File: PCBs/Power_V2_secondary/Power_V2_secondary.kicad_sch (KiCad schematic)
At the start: 9 parts, among them IC7 ACS712ELCTR-20A-T, J1 PCIE-164-02-F-D-TH-TR, J15 YK4420203000G, J8 Conn_01x02, U2 178.6164.0001

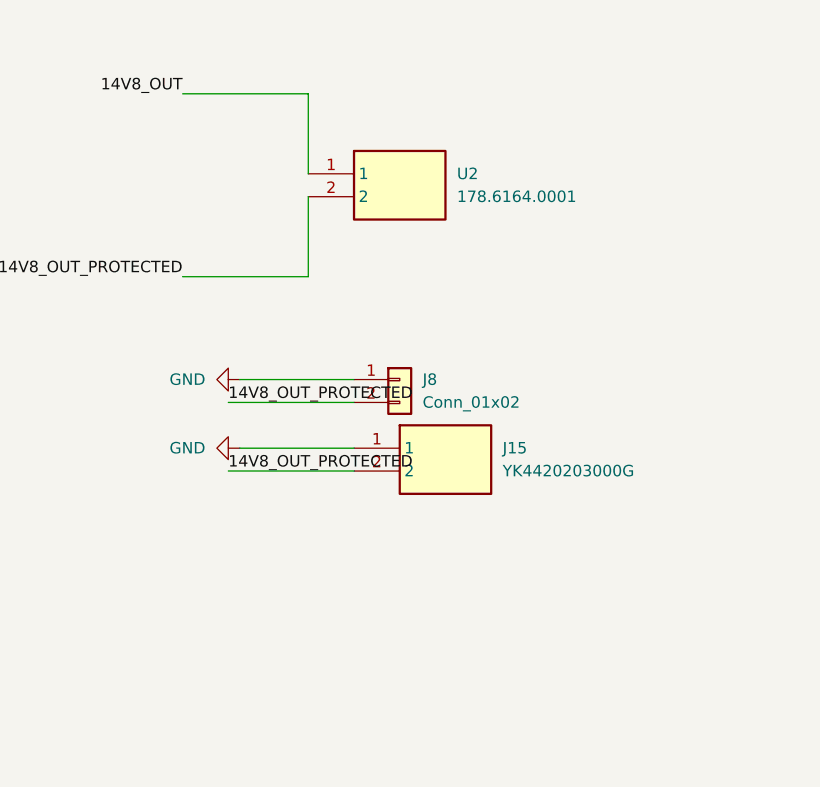
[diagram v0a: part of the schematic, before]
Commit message: shortened main board and secondary
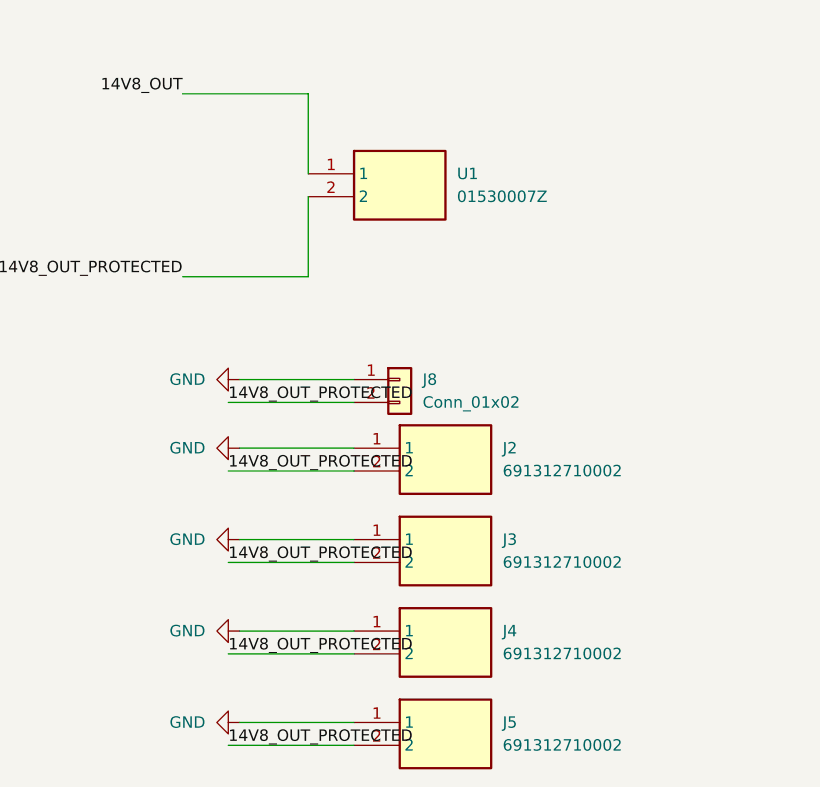
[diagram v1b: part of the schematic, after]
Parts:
- removed J15: YK4420203000G, iprl_footprints:RHDR2W120P0X950_1X2_2050X1430X1790P, symbol YK4420203000G:YK4420203000G
- removed U2: 178.6164.0001, iprl_footprints:178.6164.XXX1, symbol 178_6164_0001:178.6164.0001
- added J2, J3, J4, J5: 691312710002, iprl_footprints:SHDR2W100P0X500_1X2_1000X1200X850P, symbol 691312710002:691312710002
- added U1: 01530007Z, iprl_footprints:01530007Z, symbol 01530007Z:01530007Z
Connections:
- net 14V8_OUT: now also U1.1
- net 14V8_OUT_PROTECTED: now also J2.2, J3.2, J4.2, J5.2, U1.2
- net GND: now also J2.1, J3.1, J4.1, J5.1

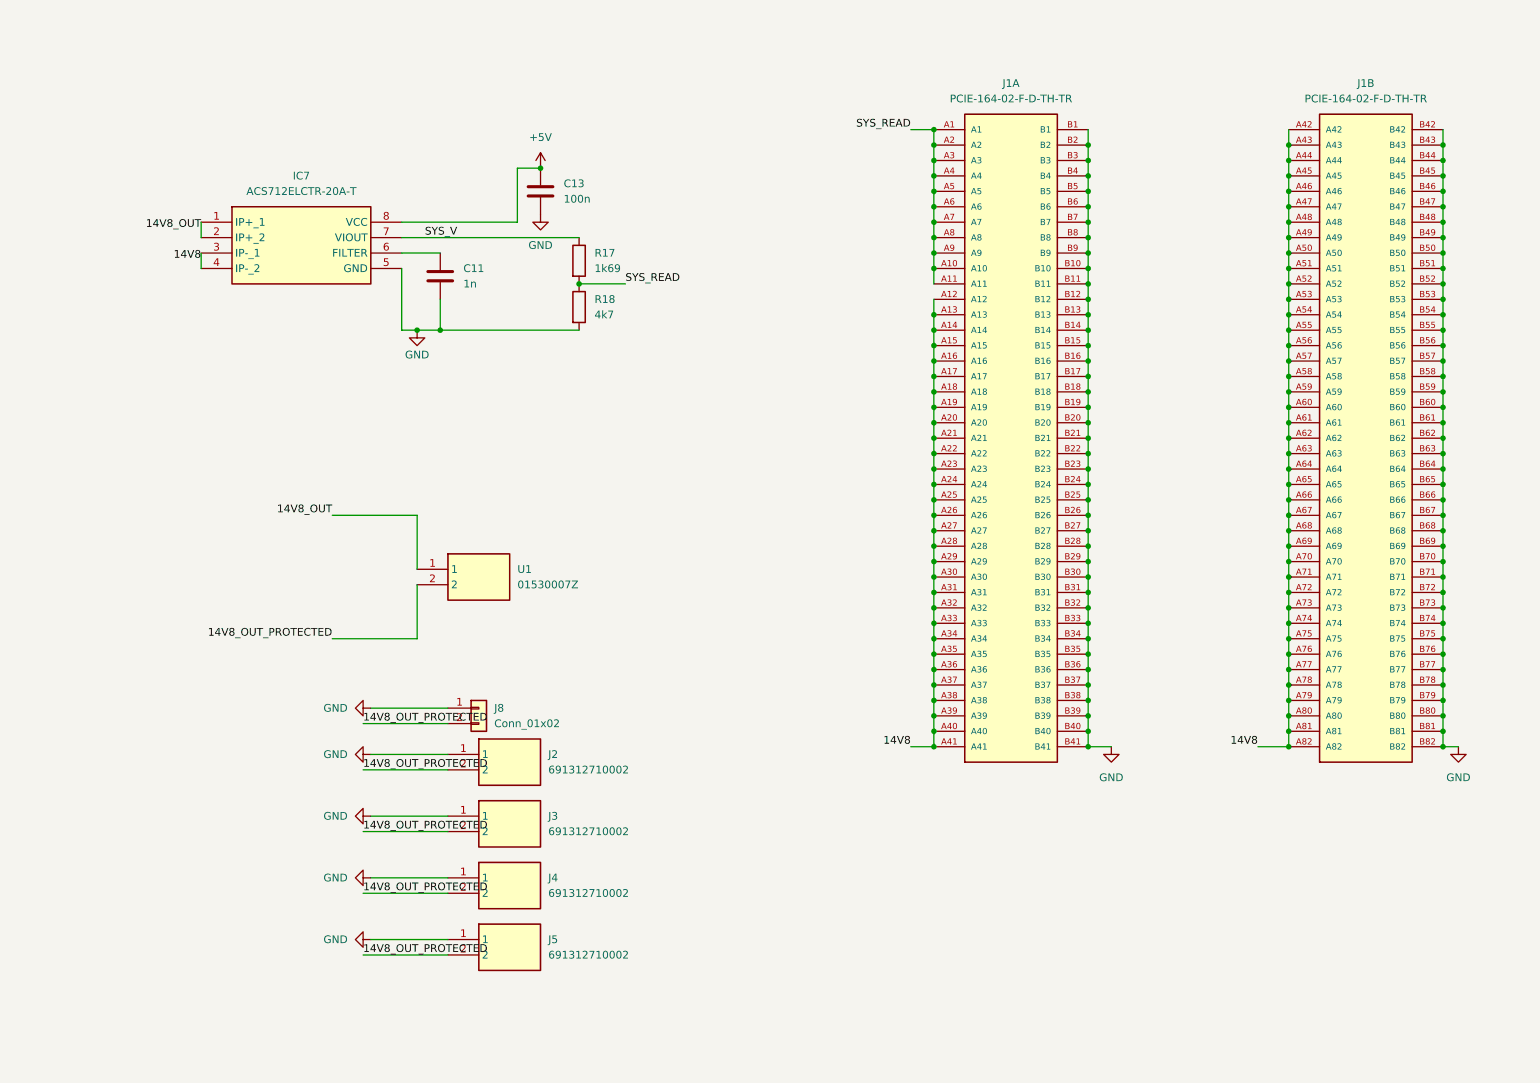
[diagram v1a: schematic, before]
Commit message: LEDs added to secondary
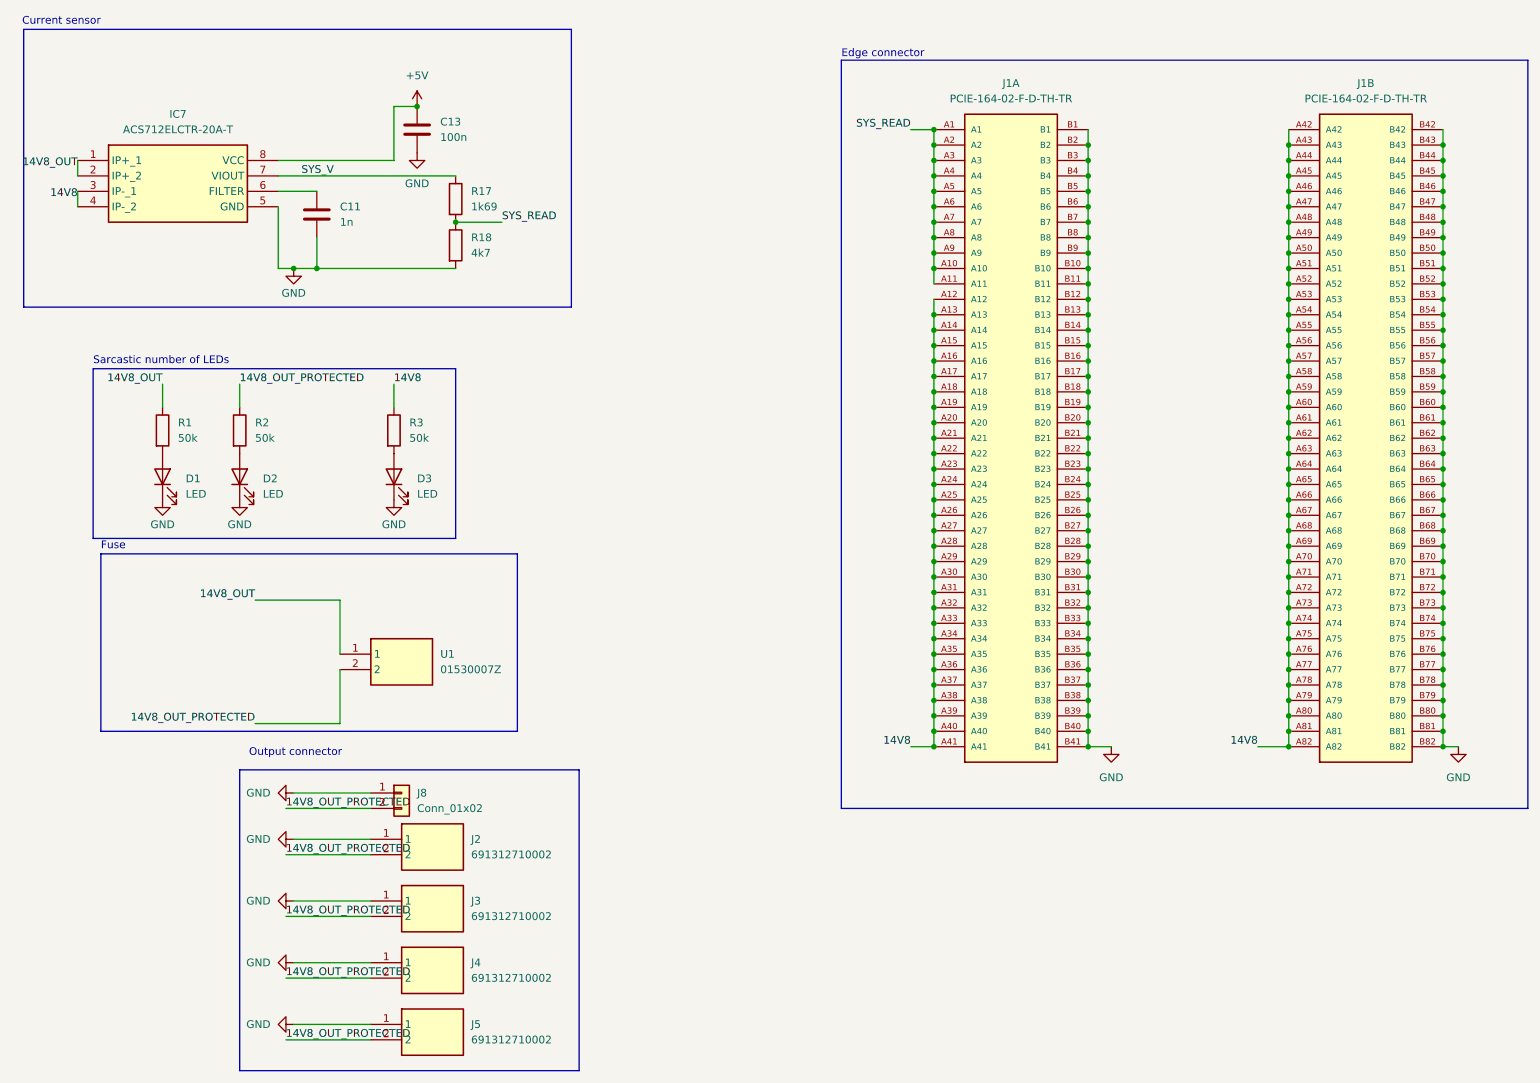
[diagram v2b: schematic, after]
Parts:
- added D1, D2, D3: LED, Diode_SMD:D_0805_2012Metric, symbol Device:LED
- added R1, R2, R3: 50k, Resistor_SMD:R_0805_2012Metric, symbol Device:R
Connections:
- net 14V8: now also R3.1
- net 14V8_OUT: now also R1.1
- net 14V8_OUT_PROTECTED: now also R2.1
- net GND: now also D1.1 (K), D2.1 (K), D3.1 (K)
- new net: D1.2 (A), R1.2
- new net: D3.2 (A), R3.2
- new net: D2.2 (A), R2.2
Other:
- note added: "Current sensor"
- note added: "Edge connector"
- note added: "Fuse"
- note added: "Output connector"
- note added: "Sarcastic number of LEDs"
- moved on the sheet: C11, C13, IC7, J2, J3, J4, J5, J8, R17, R18, U1

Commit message: added LED indicators to board and redid power distribution in PCIe
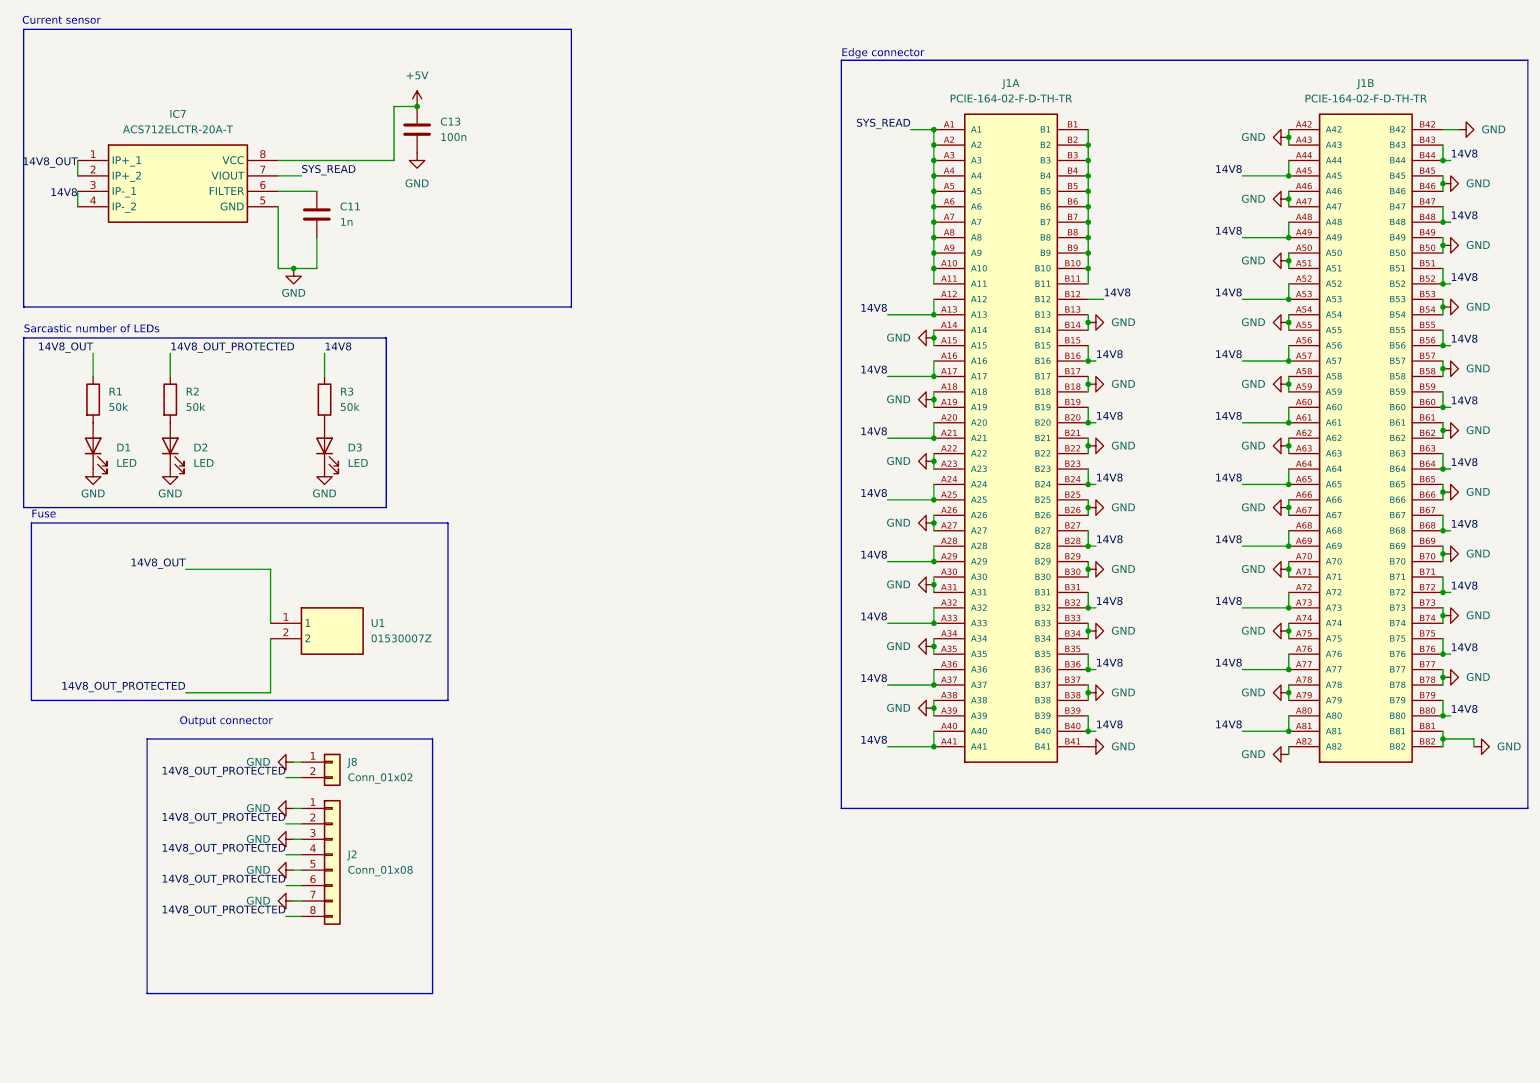
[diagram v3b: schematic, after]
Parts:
- removed J2, J3, J4, J5: 691312710002, iprl_footprints:SHDR2W100P0X500_1X2_1000X1200X850P, symbol 691312710002:691312710002
- removed R17: 1k69, Resistor_SMD:R_0805_2012Metric, symbol Device:R
- removed R18: 4k7, Resistor_SMD:R_0805_2012Metric, symbol Device:R
- added J2: Conn_01x08, TerminalBlock:TerminalBlock_MaiXu_MX126-5.0-08P_1x08_P5.00mm, symbol Connector_Generic:Conn_01x08
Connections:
- net SYS_V is gone; now on net SYS_READ: IC7.7 (VIOUT)
- net 14V8: now also J1.B12, J1.B15, J1.B16, J1.B19, J1.B20, J1.B23, J1.B24, J1.B27, J1.B28, J1.B31, J1.B32, J1.B35, J1.B36, J1.B39, J1.B40, J1.B43, J1.B44, J1.B47, J1.B48, J1.B51, J1.B52, J1.B55, J1.B56, J1.B59, J1.B60, J1.B63, J1.B64, J1.B67, J1.B68, J1.B71, J1.B72, J1.B75, J1.B76, J1.B79, J1.B80; no longer J1.A14, J1.A15, J1.A18, J1.A19, J1.A22, J1.A23, J1.A26, J1.A27, J1.A30, J1.A31, J1.A34, J1.A35, J1.A38, J1.A39, J1.A42, J1.A43, J1.A46, J1.A47, J1.A50, J1.A51, J1.A54, J1.A55, J1.A58, J1.A59, J1.A62, J1.A63, J1.A66, J1.A67, J1.A70, J1.A71, J1.A74, J1.A75, J1.A78, J1.A79, J1.A82
- net 14V8_OUT_PROTECTED: now also J2.2 (Pin_2), J2.4 (Pin_4), J2.6 (Pin_6), J2.8 (Pin_8)
- net GND: now also J1.A14, J1.A15, J1.A18, J1.A19, J1.A22, J1.A23, J1.A26, J1.A27, J1.A30, J1.A31, J1.A34, J1.A35, J1.A38, J1.A39, J1.A42, J1.A43, J1.A46, J1.A47, J1.A50, J1.A51, J1.A54, J1.A55, J1.A58, J1.A59, J1.A62, J1.A63, J1.A66, J1.A67, J1.A70, J1.A71, J1.A74, J1.A75, J1.A78, J1.A79, J1.A82, J2.1 (Pin_1), J2.3 (Pin_3), J2.5 (Pin_5), J2.7 (Pin_7); no longer J1.B1, J1.B10, J1.B11, J1.B12, J1.B15, J1.B16, J1.B19, J1.B2, J1.B20, J1.B23, J1.B24, J1.B27, J1.B28, J1.B3, J1.B31, J1.B32, J1.B35, J1.B36, J1.B39, J1.B4, J1.B40, J1.B43, J1.B44, J1.B47, J1.B48, J1.B5, J1.B51, J1.B52, J1.B55, J1.B56, J1.B59, J1.B6, J1.B60, J1.B63, J1.B64, J1.B67, J1.B68, J1.B7, J1.B71, J1.B72, J1.B75, J1.B76, J1.B79, J1.B8, J1.B80, J1.B9
- new net: J1.B1, J1.B10, J1.B11, J1.B2, J1.B3, J1.B4, J1.B5, J1.B6, J1.B7, J1.B8, J1.B9
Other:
- moved on the sheet: D1, D2, D3, J8, R1, R2, R3, U1

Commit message: added mounting holes to secondary
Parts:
- added H1, H2: MountingHole, MountingHole:MountingHole_2.5mm, symbol Mechanical:MountingHole
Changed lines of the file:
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@@
+	)
+	(symbol
+		(lib_id "Mechanical:MountingHole")
+		(at 107.95 80.01 0)
+		(unit 1)
+		(exclude_from_sim no)
+		(in_bom no)
+		(on_board yes)
+		(dnp no)
+		(fields_autoplaced yes)
+		(property "Reference" "H2"
+			(at 110.49 78.7399 0)
+			(effects
+				(font
+					(size 1.27 1.27)
+				)
+				(justify left)
+			)
+		)
+		(property "Value" "MountingHole"
+			(at 110.49 81.2799 0)
+			(effects
+				(font
+					(size 1.27 1.27)
+				)
+				(justify left)
+			)
+		)
+		(property "Footprint" "MountingHole:MountingHole_2.5mm"
+			(at 107.95 80.01 0)
+			(effects
+				(font
+					(size 1.27 1.27)
+				)
+				(hide yes)
+			)
+		)
+		(property "Datasheet" "~"
+			(at 107.95 80.01 0)
+			(effects
+				(font
+					(size 1.27 1.27)
+				)
+				(hide yes)
+			)
+		)
+		(property "Description" "Mounting Hole without connection"
+			(at 107.95 80.01 0)
+			(effects
+				(font
+					(size 1.27 1.27)
+				)
+				(hide yes)
+			)
+		)
+		(instances
+			(project "Power_V2_secondary"
+				(path "/5d5051fd-2bba-4f17-ac84-ab8502b20b0d"
+					(reference "H2")
+					(unit 1)
+				)
+			)
+		)
 	)
 	(symbol
@@
 					(unit 1)
 				)
+			)
+		)
+	)
+	(symbol
+		(lib_id "Mechanical:MountingHole")
+		(at 92.71 80.01 0)
+		(unit 1)
+		(exclude_from_sim no)
+		(in_bom no)
+		(on_board yes)
+		(dnp no)
+		(fields_autoplaced yes)
+		(property "Reference" "H1"
+			(at 95.25 78.7399 0)
+			(effects
+				(font
+					(size 1.27 1.27)
+				)
+				(justify left)
+			)
+		)
+		(property "Value" "MountingHole"
+			(at 95.25 81.2799 0)
+			(effects
+				(font
+					(size 1.27 1.27)
+				)
+				(justify left)
+			)
+		)
+		(property "Footprint" "MountingHole:MountingHole_2.5mm"
+			(at 92.71 80.01 0)
+			(effects
+				(font
+					(size 1.27 1.27)
+				)
+				(hide yes)
+			)
+		)
+		(property "Datasheet" "~"
+			(at 92.71 80.01 0)
+			(effects
+				(font
+					(size 1.27 1.27)
+				)
+				(hide yes)
+			)
+		)
+		(property "Description" "Mounting Hole without connection"
+			(at 92.71 80.01 0)
+			(effects
+				(font
+					(size 1.27 1.27)
+				)
+				(hide yes)
+			)
+		)
+		(instances
+			(project "Power_V2_secondary"
+				(path "/5d5051fd-2bba-4f17-ac84-ab8502b20b0d"
+					(reference "H1")
+					(unit 1)
+				)

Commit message: Changes from meeting
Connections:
- net GND: now also J1.B1, J1.B10, J1.B11, J1.B2, J1.B3, J1.B4, J1.B5, J1.B6, J1.B7, J1.B8, J1.B9
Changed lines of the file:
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@@
 	)
 	(junction
+		(at 193.04 33.02)
+		(diameter 0)
+		(color 0 0 0 0)
+	)
+	(junction
 		(at 167.64 128.27)
 		(diameter 0)
@@
 	(wire
 		(pts
-			(xy 193.04 40.64) (xy 193.04 43.18)
+			(xy 167.64 111.76) (xy 167.64 114.3)
 		)
 		(stroke
@@
 	(wire
 		(pts
-			(xy 167.64 111.76) (xy 167.64 114.3)
+			(xy 251.46 101.6) (xy 251.46 102.87)
 		)
 		(stroke
@@
 	(wire
 		(pts
-			(xy 251.46 101.6) (xy 251.46 102.87)
+			(xy 193.04 74.93) (xy 193.04 76.2)
 		)
 		(stroke
@@
 	(wire
 		(pts
-			(xy 193.04 74.93) (xy 193.04 76.2)
+			(xy 251.46 76.2) (xy 251.46 78.74)
 		)
 		(stroke
@@
 	(wire
 		(pts
-			(xy 251.46 76.2) (xy 251.46 78.74)
+			(xy 193.04 33.02) (xy 195.58 33.02)
 		)
 		(stroke
@@
 	(wire
 		(pts
+			(xy 193.04 38.1) (xy 193.04 40.64)
+		)
+		(stroke
+			(width 0)
+			(type default)
+		)
+	)
+	(wire
+		(pts
 			(xy 226.06 105.41) (xy 226.06 106.68)
 		)
@@
 	(wire
 		(pts
+			(xy 193.04 50.8) (xy 193.04 53.34)
+		)
+		(stroke
+			(width 0)
+			(type default)
+		)
+	)
+	(wire
+		(pts
 			(xy 251.46 33.02) (xy 254 33.02)
 		)
@@
 	(wire
 		(pts
+			(xy 193.04 33.02) (xy 193.04 35.56)
+		)
+		(stroke
+			(width 0)
+			(type default)
+		)
+	)
+	(wire
+		(pts
 			(xy 226.06 68.58) (xy 226.06 71.12)
 		)
@@
 	(wire
 		(pts
-			(xy 193.04 38.1) (xy 193.04 40.64)
+			(xy 226.06 115.57) (xy 226.06 116.84)
 		)
 		(stroke
@@
 	(wire
 		(pts
-			(xy 226.06 115.57) (xy 226.06 116.84)
+			(xy 226.06 88.9) (xy 226.06 91.44)
 		)
 		(stroke
@@
 	(wire
 		(pts
-			(xy 226.06 88.9) (xy 226.06 91.44)
+			(xy 193.04 40.64) (xy 193.04 43.18)
 		)
 		(stroke
@@
 	(wire
 		(pts
-			(xy 193.04 50.8) (xy 193.04 53.34)
-		)
-		(stroke
-			(width 0)
-			(type default)
-		)
-	)
-	(wire
-		(pts
 			(xy 167.64 38.1) (xy 167.64 35.56)
 		)
@@
 	(wire
 		(pts
-			(xy 193.04 45.72) (xy 193.04 48.26)
-		)
-		(stroke
-			(width 0)
-			(type default)
-		)
-	)
-	(wire
-		(pts
 			(xy 226.06 64.77) (xy 226.06 66.04)
 		)
@@
 	(wire
 		(pts
-			(xy 193.04 33.02) (xy 193.04 35.56)
-		)
-		(stroke
-			(width 0)
-			(type default)
-		)
-	)
-	(wire
-		(pts
 			(xy 195.58 60.96) (xy 193.04 60.96)
 		)
@@
 	(wire
 		(pts
+			(xy 193.04 45.72) (xy 193.04 48.26)
+		)
+		(stroke
+			(width 0)
+			(type default)
+		)
+	)
+	(wire
+		(pts
 			(xy 251.46 66.04) (xy 251.46 68.58)
 		)
@@
 					(unit 1)
 				)
+			)
+		)
+	)
+	(symbol
+		(lib_id "power:GND")
+		(at 195.58 33.02 90)
+		(mirror x)
+		(unit 1)
+		(exclude_from_sim no)
+		(in_bom yes)
+		(on_board yes)
+		(dnp no)
+		(property "Reference" "#PWR0147"
+			(at 201.93 33.02 0)
+			(effects
+				(font
+					(size 1.27 1.27)
+				)
+				(hide yes)
+			)
+		)
+		(property "Value" "GND"
+			(at 199.39 33.0199 90)
+			(effects
+				(font
+					(size 1.27 1.27)
+				)
+				(justify right)
+			)
+		)
+		(property "Footprint" ""
+			(at 195.58 33.02 0)
+			(effects
+				(font
+					(size 1.27 1.27)
+				)
+				(hide yes)
+			)
+		)
+		(property "Datasheet" ""
+			(at 195.58 33.02 0)
+			(effects
+				(font
+					(size 1.27 1.27)
+				)
+				(hide yes)
+			)
+		)
+		(property "Description" "Power symbol creates a global label with name \"GND\" , ground"
+			(at 195.58 33.02 0)
+			(effects
+				(font
+					(size 1.27 1.27)
+				)
+				(hide yes)
+			)
+		)
+		(pin "1"
+		)
+		(instances
+			(project "Power_V2_secondary"
+				(path "/5d5051fd-2bba-4f17-ac84-ab8502b20b0d"
+					(reference "#PWR0147")
+					(unit 1)
+				)
